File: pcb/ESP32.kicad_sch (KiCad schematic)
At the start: 25 parts, among them J5 SPKR, SW1 BOOT, SW2 RESET, U1 SN74LV1T34DBV, U3 MAX98357A, U6 ESP32-S3-WROOM-2-N32R16V

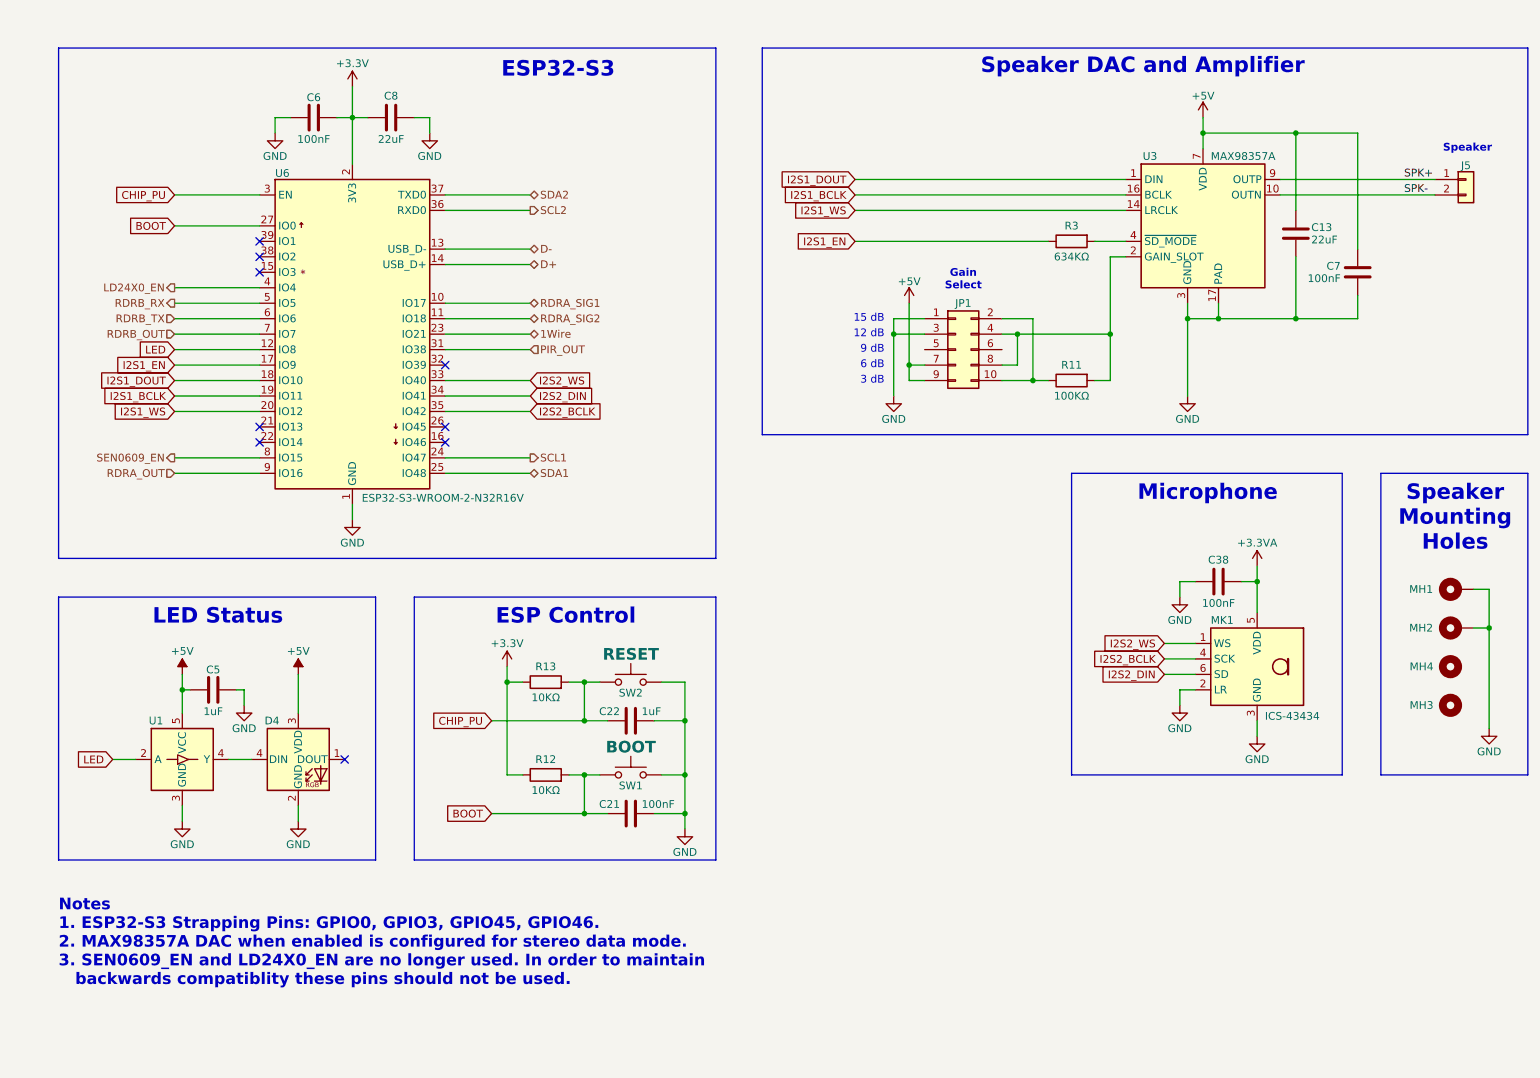
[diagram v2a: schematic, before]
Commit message: Add new ina228 to other power supplies
Not finished
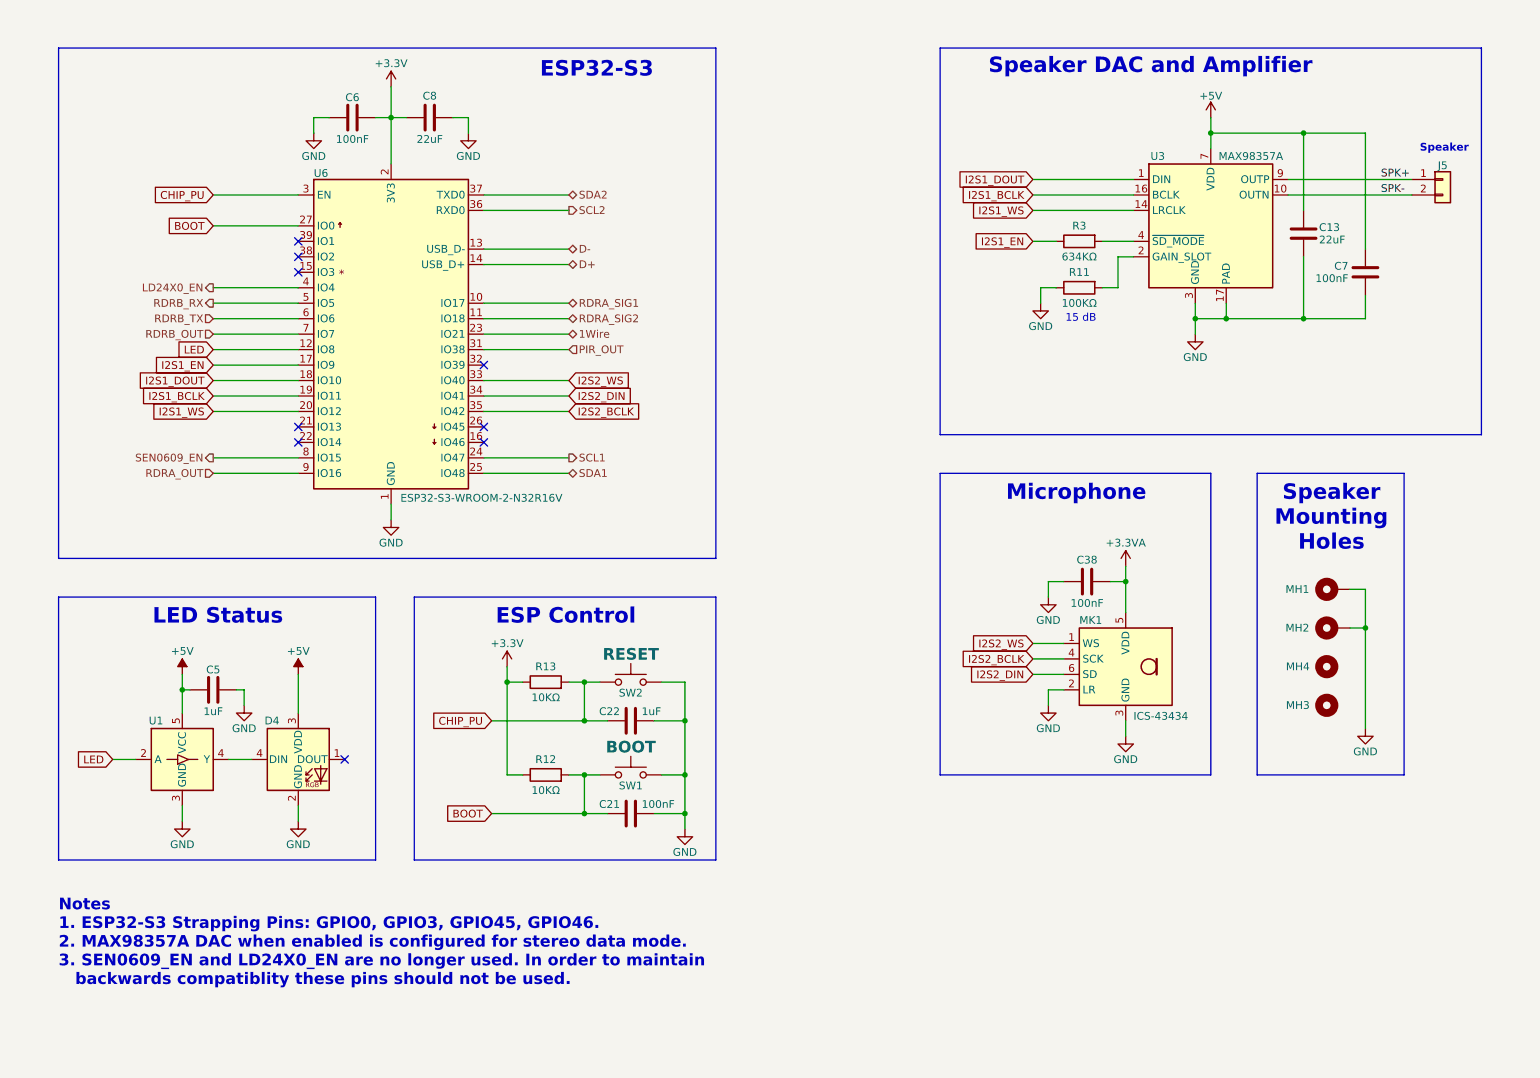
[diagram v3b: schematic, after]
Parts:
- removed JP1: Gain, TMM-105-01-X-D-SM:SAMTEC_TMM-105-01-X-D-SM, symbol Connector_Generic:Conn_02x05_Odd_Even
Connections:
- net GND: now also R11.1
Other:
- note removed: "12 dB"
- note removed: "3 dB"
- note removed: "6 dB"
- note removed: "9 dB"
- note removed: "Gain Select"
- moved on the sheet: C13, C38, C6, C7, C8, J5, MH1, MH2, MH3, MH4, MK1, R11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

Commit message: Rev B Updates finish adding power monitors for 3.3V and 3.3VA
Removed speaker gain jumper
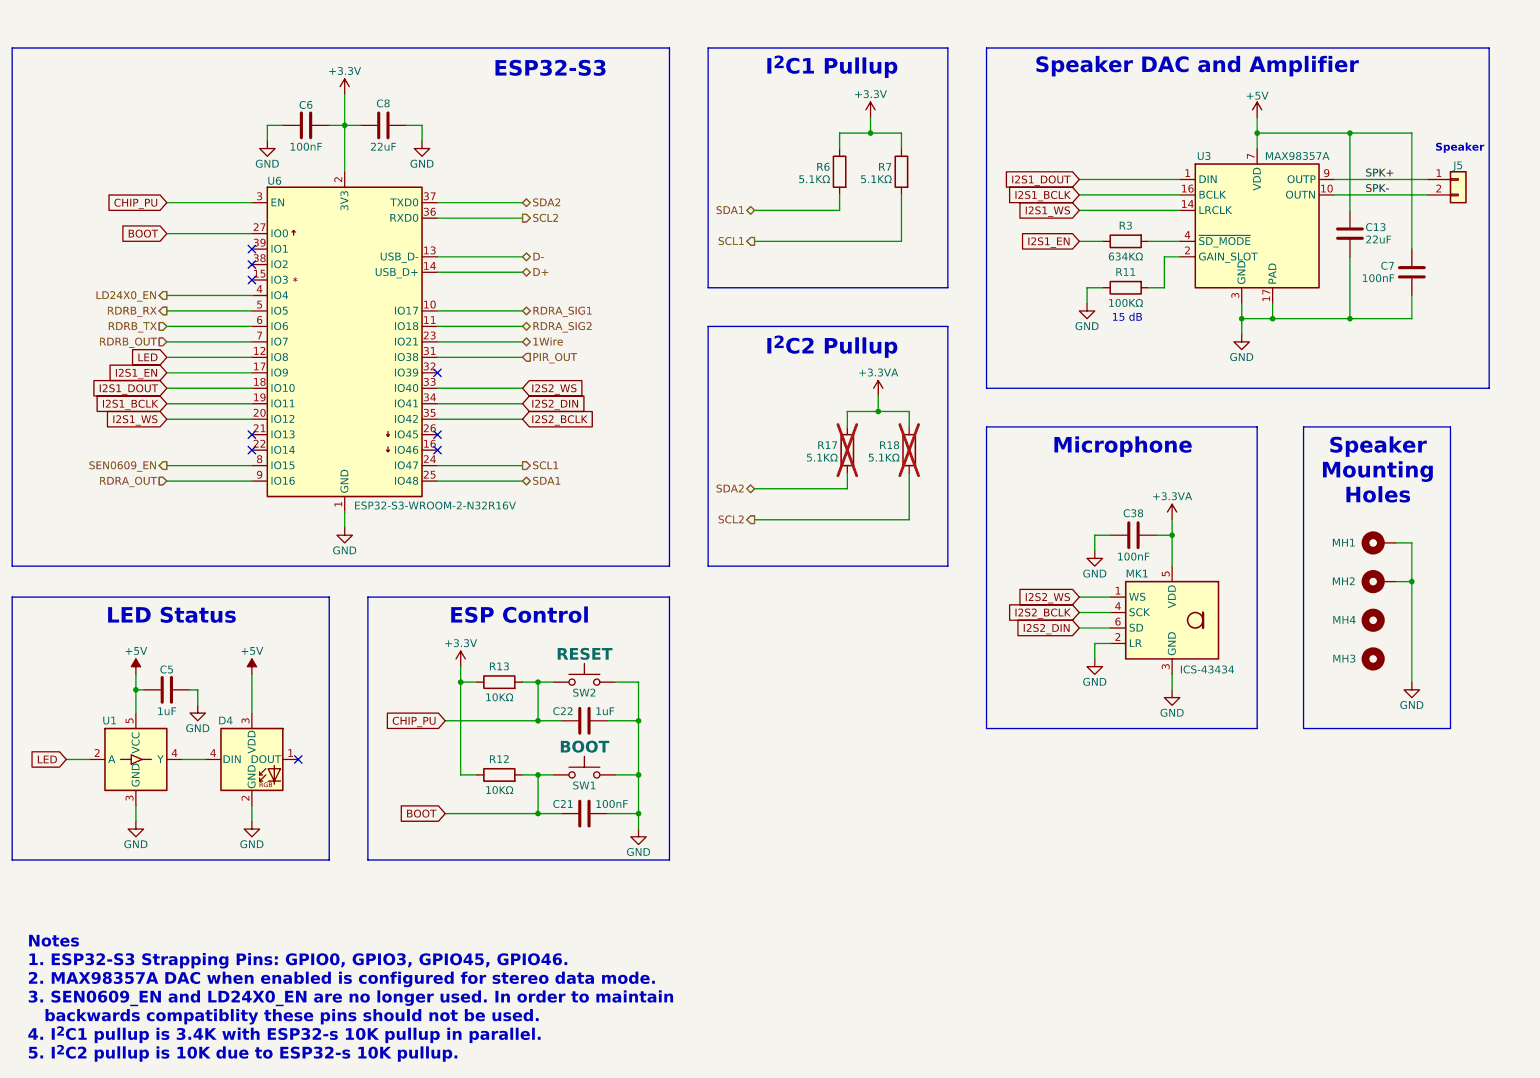
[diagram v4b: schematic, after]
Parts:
- added R17, R18, R6, R7: 5.1KΩ, Resistor_SMD:R_0402_1005Metric, symbol Device:R
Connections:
- net +3.3V: now also R6.1, R7.1
- net +3.3VA: now also R17.1, R18.1
- net SCL1: now also R7.2
- net SCL2: now also R18.2
- net SDA1: now also R6.2
- net SDA2: now also R17.2
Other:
- note added: "I^{2}C1 Pullup"
- note added: "I^{2}C2 Pullup"
- note added: "Notes 1. ESP32-S3 Strapping Pins: GPIO0, GPIO3, GPIO45, GPIO46. 2. MAX98357A DAC when enabled is configured for stereo data mode. 3. SEN0609_EN and LD24X0_EN are no longer used. In order to maintain backwards compatiblity these pins should not be used. 4. I^{2}C1 pullup is 3.4K with ESP32-s 10K pullup in parallel. 5. I^{2}C2 pullup is 10K due to ESP32-s 10K pullup."
- note removed: "Notes 1. ESP32-S3 Strapping Pins: GPIO0, GPIO3, GPIO45, GPIO46. 2. MAX98357A DAC when enabled is configured for stereo data mode. 3. SEN0609_EN and LD24X0_EN are no longer used. In order to maintain backwards compatiblity these pins should not be used."
- title: ESPHome Parking Assistant -> ESPHome Indoor Multi-Sensor
- moved on the sheet: C13, C21, C22, C38, C5, C6, C7, C8, D4, J5, MH1, MH2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
